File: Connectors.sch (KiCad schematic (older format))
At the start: 4 parts

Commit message: symbol rearrangement
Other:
- moved on the sheet: J?
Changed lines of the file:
@@
 L Connector_Generic:Conn_01x09 J?
 U 1 1 5E8D1351
-P 4350 3400
-F 0 "J?" H 4430 3442 50  0000 L CNN
-F 1 "Conn_01x09" H 4430 3351 50  0000 L CNN
-F 2 "" H 4350 3400 50  0001 C CNN
-F 3 "~" H 4350 3400 50  0001 C CNN
-	1    4350 3400
+P 5300 4150
+F 0 "J?" H 5380 4192 50  0000 L CNN
+F 1 "Conn_01x09" H 5380 4101 50  0000 L CNN
+F 2 "" H 5300 4150 50  0001 C CNN
+F 3 "~" H 5300 4150 50  0001 C CNN
+	1    5300 4150
 	1    0    0    -1
 $EndComp
@@
 L Connector_Generic:Conn_01x04 J?
 U 1 1 5E8D218F
-P 5450 3100
-F 0 "J?" H 5530 3092 50  0000 L CNN
-F 1 "Conn_01x04" H 5530 3001 50  0000 L CNN
-F 2 "" H 5450 3100 50  0001 C CNN
-F 3 "~" H 5450 3100 50  0001 C CNN
-	1    5450 3100
+P 6850 3050
+F 0 "J?" H 6930 3042 50  0000 L CNN
+F 1 "Conn_01x04" H 6930 2951 50  0000 L CNN
+F 2 "" H 6850 3050 50  0001 C CNN
+F 3 "~" H 6850 3050 50  0001 C CNN
+	1    6850 3050
 	1    0    0    -1
 $EndComp
@@
 L Connector_Generic:Conn_02x03_Odd_Even J?
 U 1 1 5E8D3116
-P 4300 4650
-F 0 "J?" H 4350 4967 50  0000 C CNN
-F 1 "Conn_02x03_Odd_Even" H 4350 4876 50  0000 C CNN
-F 2 "" H 4300 4650 50  0001 C CNN
-F 3 "~" H 4300 4650 50  0001 C CNN
-	1    4300 4650
+P 6700 4300
+F 0 "J?" H 6750 4617 50  0000 C CNN
+F 1 "Conn_02x03_Odd_Even" H 6750 4526 50  0000 C CNN
+F 2 "" H 6700 4300 50  0001 C CNN
+F 3 "~" H 6700 4300 50  0001 C CNN
+	1    6700 4300
 	1    0    0    -1
 $EndComp
@@
 L Connector_Generic:Conn_01x04 J?
 U 1 1 5E8D3C74
-P 5450 4500
-F 0 "J?" H 5530 4492 50  0000 L CNN
-F 1 "Conn_01x04" H 5530 4401 50  0000 L CNN
-F 2 "" H 5450 4500 50  0001 C CNN
-F 3 "~" H 5450 4500 50  0001 C CNN
-	1    5450 4500
+P 5300 3000
+F 0 "J?" H 5380 2992 50  0000 L CNN
+F 1 "Conn_01x04" H 5380 2901 50  0000 L CNN
+F 2 "" H 5300 3000 50  0001 C CNN
+F 3 "~" H 5300 3000 50  0001 C CNN
+	1    5300 3000
 	1    0    0    -1
 $EndComp

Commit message: Annotate
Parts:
- gave numbers to parts that had none: 4
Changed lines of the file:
@@
 $EndDescr
 $Comp
-L Connector_Generic:Conn_01x09 J?
+L Connector_Generic:Conn_01x09 J2
 U 1 1 5E8D1351
 P 5300 4150
-F 0 "J?" H 5380 4192 50  0000 L CNN
+F 0 "J2" H 5380 4192 50  0000 L CNN
 F 1 "Conn_01x09" H 5380 4101 50  0000 L CNN
 F 2 "" H 5300 4150 50  0001 C CNN
@@
 $EndComp
 $Comp
-L Connector_Generic:Conn_01x04 J?
+L Connector_Generic:Conn_01x04 J4
 U 1 1 5E8D218F
 P 6850 3050
-F 0 "J?" H 6930 3042 50  0000 L CNN
+F 0 "J4" H 6930 3042 50  0000 L CNN
 F 1 "Conn_01x04" H 6930 2951 50  0000 L CNN
 F 2 "" H 6850 3050 50  0001 C CNN
@@
 $EndComp
 $Comp
-L Connector_Generic:Conn_02x03_Odd_Even J?
+L Connector_Generic:Conn_02x03_Odd_Even J3
 U 1 1 5E8D3116
 P 6700 4300
-F 0 "J?" H 6750 4617 50  0000 C CNN
+F 0 "J3" H 6750 4617 50  0000 C CNN
 F 1 "Conn_02x03_Odd_Even" H 6750 4526 50  0000 C CNN
 F 2 "" H 6700 4300 50  0001 C CNN
@@
 $EndComp
 $Comp
-L Connector_Generic:Conn_01x04 J?
+L Connector_Generic:Conn_01x04 J1
 U 1 1 5E8D3C74
 P 5300 3000
-F 0 "J?" H 5380 2992 50  0000 L CNN
+F 0 "J1" H 5380 2992 50  0000 L CNN
 F 1 "Conn_01x04" H 5380 2901 50  0000 L CNN
 F 2 "" H 5300 3000 50  0001 C CNN

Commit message: associations
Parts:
- J1: renamed from J2; value Conn_01x09 -> Digital Pins; footprint (none) -> Connector_PinSocket_2.54mm:PinSocket_1x09_P2.54mm_Vertical
- J2: renamed from J1; value Conn_01x04 -> Serial; footprint (none) -> Connector_PinSocket_2.54mm:PinSocket_1x04_P2.54mm_Vertical
- J3: value Conn_02x03_Odd_Even -> ICSP; footprint (none) -> Connector_PinSocket_2.54mm:PinSocket_2x03_P2.54mm_Vertical
- J4: value Conn_01x04 -> I2C; footprint (none) -> Connector_PinSocket_2.54mm:PinSocket_1x04_P2.54mm_Vertical
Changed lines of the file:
@@
 $EndDescr
 $Comp
-L Connector_Generic:Conn_01x09 J2
+L Connector_Generic:Conn_01x09 J1
 U 1 1 5E8D1351
 P 5300 4150
-F 0 "J2" H 5380 4192 50  0000 L CNN
-F 1 "Conn_01x09" H 5380 4101 50  0000 L CNN
-F 2 "" H 5300 4150 50  0001 C CNN
+F 0 "J1" H 5380 4192 50  0000 L CNN
+F 1 "Digital Pins" H 5380 4101 50  0000 L CNN
+F 2 "Connector_PinSocket_2.54mm:PinSocket_1x09_P2.54mm_Vertical" H 5300 4150 50  0001 C CNN
 F 3 "~" H 5300 4150 50  0001 C CNN
 	1    5300 4150
@@
 P 6850 3050
 F 0 "J4" H 6930 3042 50  0000 L CNN
-F 1 "Conn_01x04" H 6930 2951 50  0000 L CNN
-F 2 "" H 6850 3050 50  0001 C CNN
+F 1 "I2C" H 6930 2951 50  0000 L CNN
+F 2 "Connector_PinSocket_2.54mm:PinSocket_1x04_P2.54mm_Vertical" H 6850 3050 50  0001 C CNN
 F 3 "~" H 6850 3050 50  0001 C CNN
 	1    6850 3050
@@
 P 6700 4300
 F 0 "J3" H 6750 4617 50  0000 C CNN
-F 1 "Conn_02x03_Odd_Even" H 6750 4526 50  0000 C CNN
-F 2 "" H 6700 4300 50  0001 C CNN
+F 1 "ICSP" H 6750 4526 50  0000 C CNN
+F 2 "Connector_PinSocket_2.54mm:PinSocket_2x03_P2.54mm_Vertical" H 6700 4300 50  0001 C CNN
 F 3 "~" H 6700 4300 50  0001 C CNN
 	1    6700 4300
@@
 $EndComp
 $Comp
-L Connector_Generic:Conn_01x04 J1
+L Connector_Generic:Conn_01x04 J2
 U 1 1 5E8D3C74
 P 5300 3000
-F 0 "J1" H 5380 2992 50  0000 L CNN
-F 1 "Conn_01x04" H 5380 2901 50  0000 L CNN
-F 2 "" H 5300 3000 50  0001 C CNN
+F 0 "J2" H 5380 2992 50  0000 L CNN
+F 1 "Serial " H 5380 2901 50  0000 L CNN
+F 2 "Connector_PinSocket_2.54mm:PinSocket_1x04_P2.54mm_Vertical" H 5300 3000 50  0001 C CNN
 F 3 "~" H 5300 3000 50  0001 C CNN
 	1    5300 3000

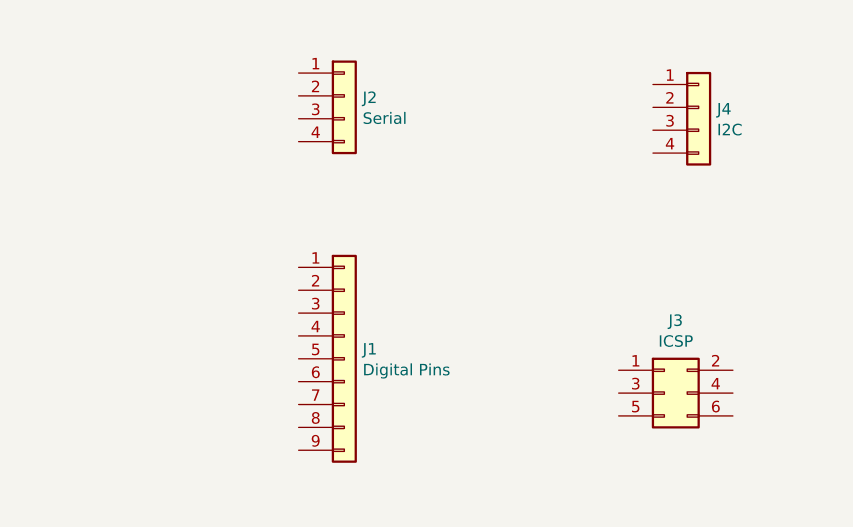
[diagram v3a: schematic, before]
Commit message: Completed wiring in connectors
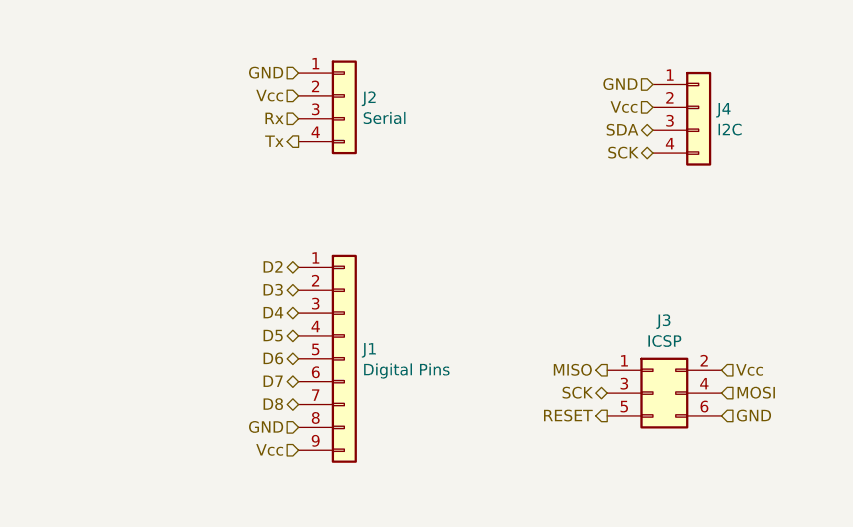
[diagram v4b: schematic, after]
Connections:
- net D2: now reaches J1.1 (Pin_1)
- net D3: now reaches J1.2 (Pin_2)
- net D4: now reaches J1.3 (Pin_3)
- net D5: now reaches J1.4 (Pin_4)
- net D6: now reaches J1.5 (Pin_5)
- net D7: now reaches J1.6 (Pin_6)
- net D8: now reaches J1.7 (Pin_7)
- net GND: now reaches J1.8 (Pin_8)
- net GND: now also J2.1 (Pin_1), J3.6 (Pin_6), J4.1 (Pin_1)
- net Vcc: now reaches J1.9 (Pin_9)
- net Vcc: now also J2.2 (Pin_2), J3.2 (Pin_2), J4.2 (Pin_2)
- net SDA: now reaches J4.3 (Pin_3)
- net SCK: now reaches J4.4 (Pin_4)
- net SCK: now also J3.3 (Pin_3)
- net MISO: now reaches J3.1 (Pin_1)
- net MOSI: now reaches J3.4 (Pin_4)
- net RESET: now reaches J3.5 (Pin_5)
- net Rx: now reaches J2.3 (Pin_3)
- net Tx: now reaches J2.4 (Pin_4)
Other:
- moved on the sheet: J3
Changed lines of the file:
@@
 L Connector_Generic:Conn_02x03_Odd_Even J3
 U 1 1 5E8D3116
-P 6700 4300
-F 0 "J3" H 6750 4617 50  0000 C CNN
-F 1 "ICSP" H 6750 4526 50  0000 C CNN
-F 2 "Connector_PinSocket_2.54mm:PinSocket_2x03_P2.54mm_Vertical" H 6700 4300 50  0001 C CNN
-F 3 "~" H 6700 4300 50  0001 C CNN
-	1    6700 4300
+P 6650 4300
+F 0 "J3" H 6700 4617 50  0000 C CNN
+F 1 "ICSP" H 6700 4526 50  0000 C CNN
+F 2 "Connector_PinSocket_2.54mm:PinSocket_2x03_P2.54mm_Vertical" H 6650 4300 50  0001 C CNN
+F 3 "~" H 6650 4300 50  0001 C CNN
+	1    6650 4300
 	1    0    0    -1
 $EndComp
@@
 	1    0    0    -1
 $EndComp
+Text HLabel 6450 4200 0    50   Output ~ 0
+MISO
+Text HLabel 6450 4300 0    50   BiDi ~ 0
+SCK
+Text HLabel 6450 4400 0    50   Output ~ 0
+RESET
+Text HLabel 6950 4200 2    50   Input ~ 0
+Vcc
+Text HLabel 6950 4300 2    50   Input ~ 0
+MOSI
+Text HLabel 6950 4400 2    50   Input ~ 0
+GND
+Text HLabel 5100 2900 0    50   Input ~ 0
+GND
+Text HLabel 5100 3000 0    50   Input ~ 0
+Vcc
+Text HLabel 5100 3100 0    50   Input ~ 0
+Rx
+Text HLabel 5100 3200 0    50   Output ~ 0
+Tx
+Text HLabel 6650 2950 0    50   Input ~ 0
+GND
+Text HLabel 6650 3050 0    50   Input ~ 0
+Vcc
+Text HLabel 6650 3150 0    50   BiDi ~ 0
+SDA
+Text HLabel 6650 3250 0    50   BiDi ~ 0
+SCK
+Text HLabel 5100 3750 0    50   BiDi ~ 0
+D2
+Text HLabel 5100 3850 0    50   BiDi ~ 0
+D3
+Text HLabel 5100 3950 0    50   BiDi ~ 0
+D4
+Text HLabel 5100 4050 0    50   BiDi ~ 0
+D5
+Text HLabel 5100 4150 0    50   BiDi ~ 0
+D6
+Text HLabel 5100 4250 0    50   BiDi ~ 0
+D7
+Text HLabel 5100 4350 0    50   BiDi ~ 0
+D8
+Text HLabel 5100 4450 0    50   Input ~ 0
+GND
+Text HLabel 5100 4550 0    50   Input ~ 0
+Vcc
 $EndSCHEMATC

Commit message: Comments
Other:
- note added: "GPIO Connector"
- note added: "I2C Connector\n"
- note added: "SPI Connector"
- note added: "Serial Connector\n"
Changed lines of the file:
@@
 Text HLabel 5100 4550 0    50   Input ~ 0
 Vcc
+Text Notes 5500 2750 2    50   ~ 0
+Serial Connector\n
+Text Notes 6950 2750 2    50   ~ 0
+I2C Connector\n
+Text Notes 5400 3600 2    50   ~ 0
+GPIO Connector
+Text Notes 6950 3850 2    50   ~ 0
+SPI Connector
 $EndSCHEMATC
